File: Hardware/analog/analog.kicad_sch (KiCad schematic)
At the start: 1 part, among them Y101 25MHz

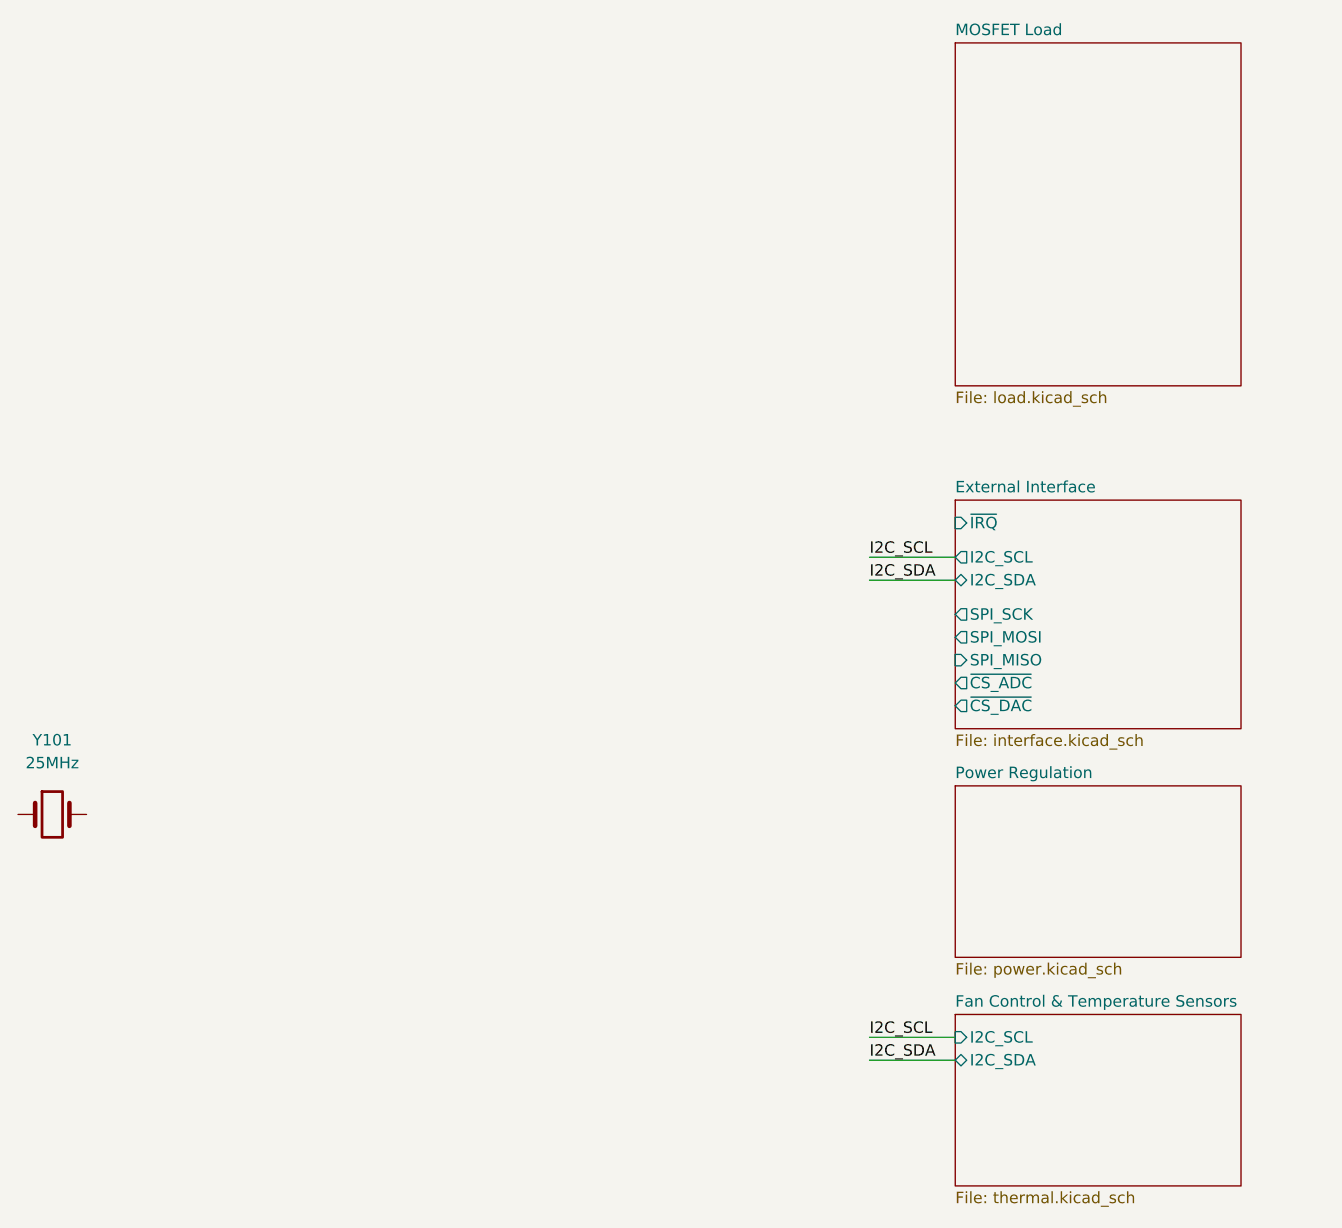
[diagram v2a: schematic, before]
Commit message: Added ADC/DAC section
- Imported the schematic for the analog DAC/ADC section, as well as the
  Vref generator and clock generator for the ADC
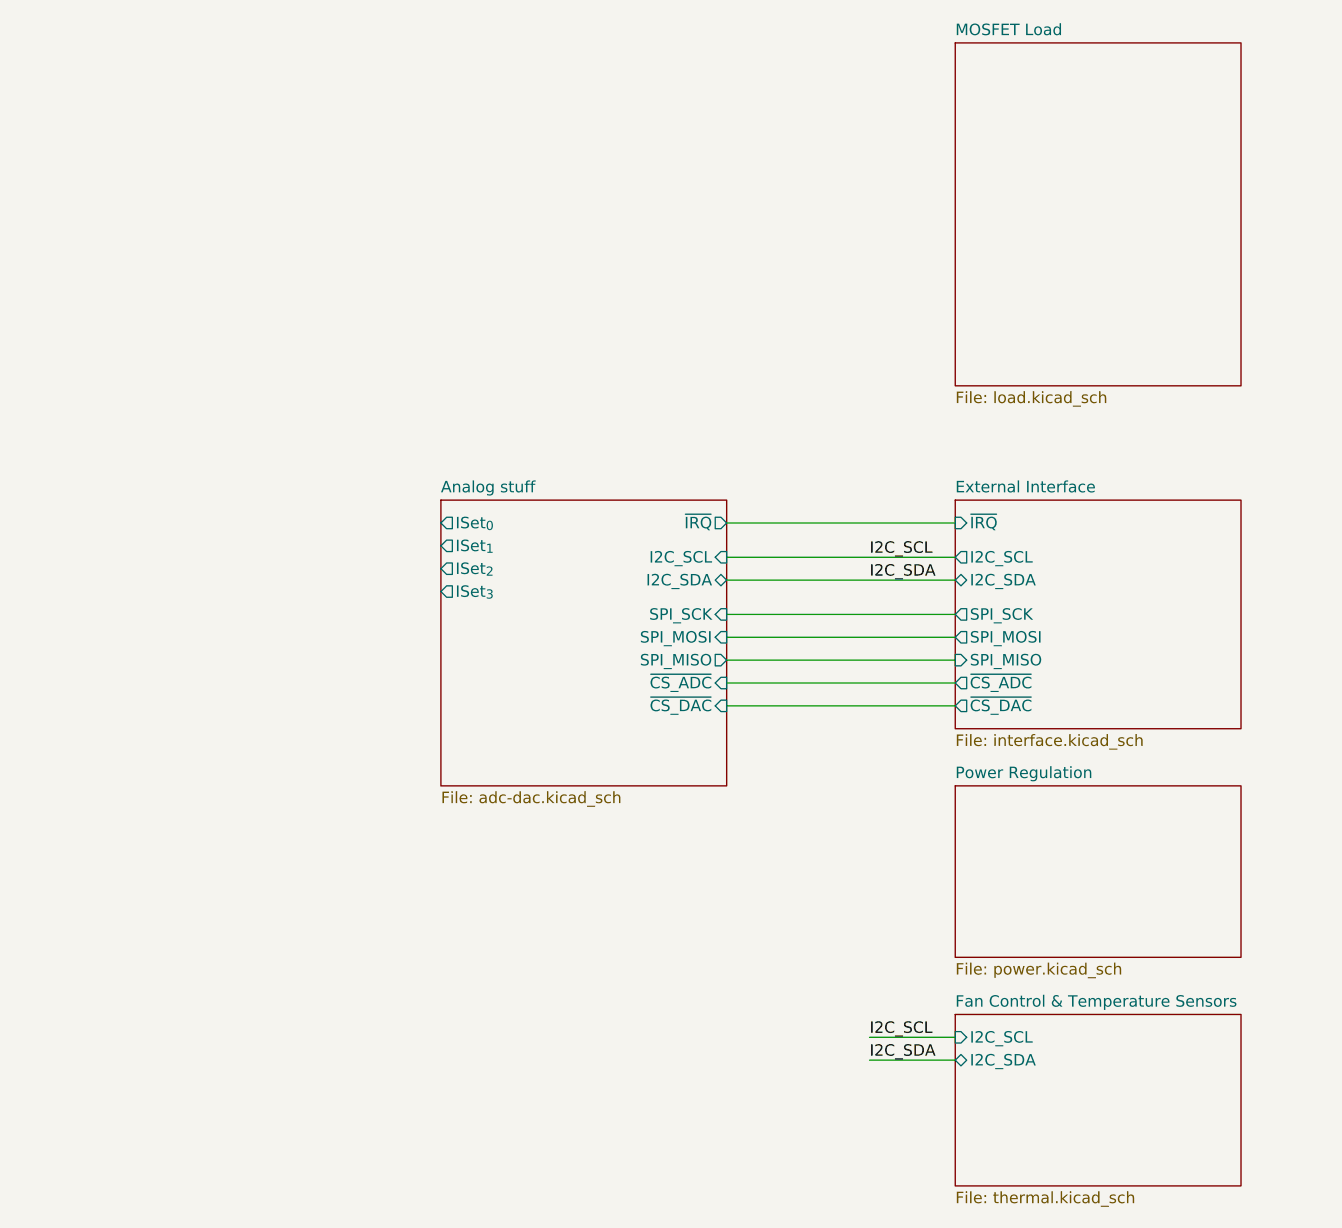
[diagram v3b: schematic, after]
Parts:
- removed Y101: 25MHz, Crystal:Crystal_SMD_SeikoEpson_TSX3225-4Pin_3.2x2.5mm_HandSoldering, symbol Device:Crystal
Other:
- added sheet Analog stuff (adc-dac.kicad_sch)

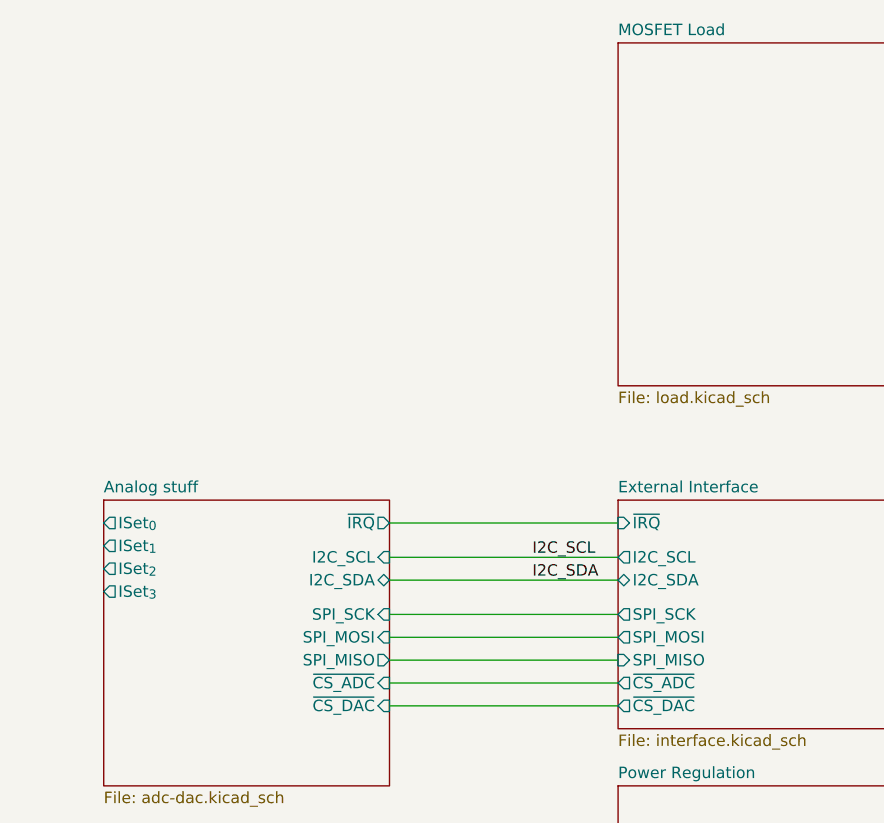
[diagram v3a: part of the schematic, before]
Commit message: Add ADC aliasing filters
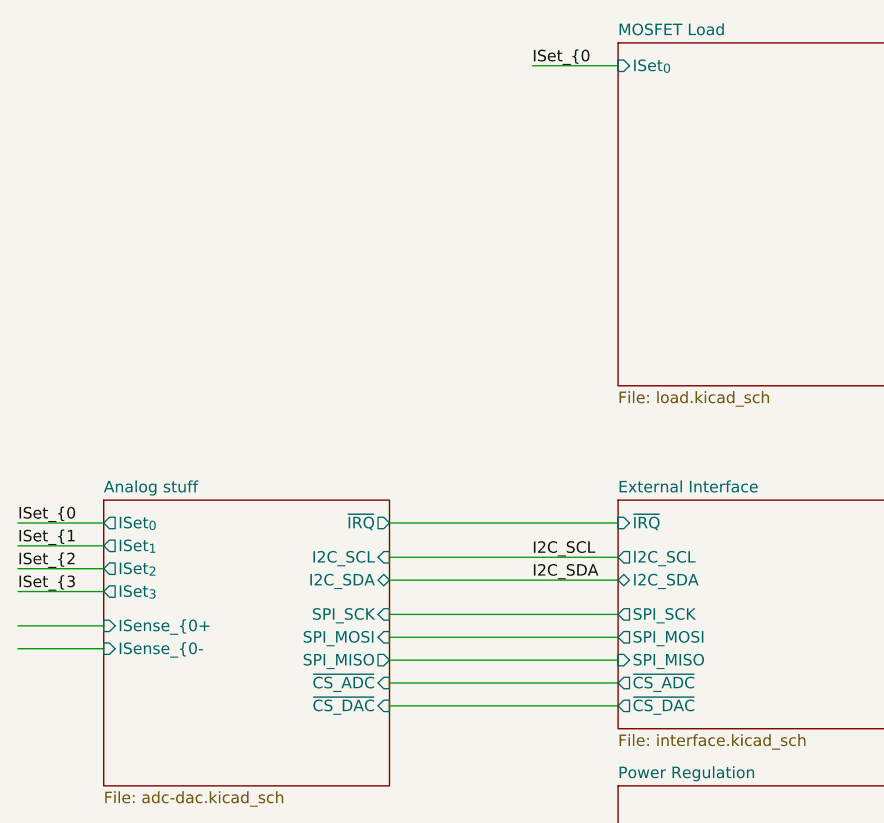
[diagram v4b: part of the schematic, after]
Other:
- sheet Analog stuff ports: added ISense_{0+, ISense_{0-; removed none
- sheet MOSFET Load ports: added ISet_{0}; removed none
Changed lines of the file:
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@@
+    (stroke (width 0) (type default) (color 0 0 0 0))
+  )
+  (wire (pts (xy 161.925 86.36) (xy 171.45 86.36))
     (stroke (width 0) (type default) (color 0 0 0 0))
   )
@@
     (stroke (width 0) (type default) (color 0 0 0 0))
   )
+  (wire (pts (xy 161.925 78.74) (xy 171.45 78.74))
+    (stroke (width 0) (type default) (color 0 0 0 0))
+  )
+  (wire (pts (xy 219.075 27.94) (xy 228.6 27.94))
+    (stroke (width 0) (type default) (color 0 0 0 0))
+  )
   (wire (pts (xy 203.2 99.06) (xy 228.6 99.06))
     (stroke (width 0) (type default) (color 0 0 0 0))
@@
     (stroke (width 0) (type default) (color 0 0 0 0))
   )
+  (wire (pts (xy 161.925 90.17) (xy 171.45 90.17))
+    (stroke (width 0) (type default) (color 0 0 0 0))
+  )
+  (wire (pts (xy 161.925 81.28) (xy 171.45 81.28))
+    (stroke (width 0) (type default) (color 0 0 0 0))
+  )
   (wire (pts (xy 203.2 96.52) (xy 228.6 96.52))
     (stroke (width 0) (type default) (color 0 0 0 0))
   )
   (wire (pts (xy 203.2 78.74) (xy 228.6 78.74))
+    (stroke (width 0) (type default) (color 0 0 0 0))
+  )
+  (wire (pts (xy 161.925 83.82) (xy 171.45 83.82))
+    (stroke (width 0) (type default) (color 0 0 0 0))
+  )
+  (wire (pts (xy 161.925 92.71) (xy 171.45 92.71))
     (stroke (width 0) (type default) (color 0 0 0 0))
   )
@@
     (effects (font (size 1.27 1.27)) (justify left bottom))
   )
+  (label "ISet_{0" (at 161.925 78.74 0)
+    (effects (font (size 1.27 1.27)) (justify left bottom))
+  )
+  (label "ISet_{2" (at 161.925 83.82 0)
+    (effects (font (size 1.27 1.27)) (justify left bottom))
+  )
   (label "I2C_SDA" (at 219.075 138.43 0)
     (effects (font (size 1.27 1.27)) (justify left bottom))
   )
+  (label "ISet_{1" (at 161.925 81.28 0)
+    (effects (font (size 1.27 1.27)) (justify left bottom))
+  )
   (label "I2C_SCL" (at 219.075 135.89 0)
+    (effects (font (size 1.27 1.27)) (justify left bottom))
+  )
+  (label "ISet_{3" (at 161.925 86.36 0)
+    (effects (font (size 1.27 1.27)) (justify left bottom))
+  )
+  (label "ISet_{0" (at 219.075 27.94 0)
     (effects (font (size 1.27 1.27)) (justify left bottom))
   )
@@
       (effects (font (size 1.27 1.27)) (justify left))
     )
+    (pin "ISense_{0+" input (at 171.45 90.17 180)
+      (effects (font (size 1.27 1.27)) (justify left))
+    )
+    (pin "ISense_{0-" input (at 171.45 92.71 180)
+      (effects (font (size 1.27 1.27)) (justify left))
+    )
   )
   (sheet (at 228.6 76.2) (size 31.75 25.4) (fields_autoplaced)
@@
     (property "Sheet file" "load.kicad_sch" (id 1) (at 228.6 64.0846 0)
       (effects (font (size 1.27 1.27)) (justify left top))
+    )
+    (pin "ISet_{0}" input (at 228.6 27.94 180)
+      (effects (font (size 1.27 1.27)) (justify left))
     )
   )
@@
       (reference "#PWR0111") (unit 1) (value "GNDA") (footprint "")
     )
+    (path "/afc218b4-6ce8-4742-9485-86399056c336/9e14dd43-0fb7-4e60-92a4-f58637916ead/c0d157c8-1a8b-4612-821d-710aff7d9c6d"
+      (reference "#PWR0112") (unit 1) (value "GND") (footprint "")
+    )
     (path "/afc218b4-6ce8-4742-9485-86399056c336/9e14dd43-0fb7-4e60-92a4-f58637916ead/e7443b7c-a1d7-4f36-833b-16f24cacd8f7"
       (reference "#PWR0113") (unit 1) (value "GND") (footprint "")
@@
       (reference "#PWR0116") (unit 1) (value "+3V3") (footprint "")
     )
+    (path "/afc218b4-6ce8-4742-9485-86399056c336/9e14dd43-0fb7-4e60-92a4-f58637916ead/6c88dc86-3465-4d2e-9993-73883be4ba7e"
+      (reference "#PWR0117") (unit 1) (value "GND") (footprint "")
+    )
+    (path "/e1649c35-e6e3-47dd-8aeb-a217676fe0ce/b5ee31ed-922a-4c24-9141-295f8bfa1a93"
+      (reference "#PWR0118") (unit 1) (value "-5VA") (footprint "")
+    )
     (path "/e1649c35-e6e3-47dd-8aeb-a217676fe0ce/d6b232d9-faf0-4a9d-8350-e9a8056ff3c8"
       (reference "#PWR0201") (unit 1) (value "GNDPWR") (footprint "")
@@
       (reference "#PWR0205") (unit 1) (value "GND") (footprint "")
     )
-    (path "/e1649c35-e6e3-47dd-8aeb-a217676fe0ce/a60ae066-97ff-47a0-9fba-29cc0372063e"
-      (reference "#PWR0206") (unit 1) (value "-5V") (footprint "")
-    )
     (path "/e1649c35-e6e3-47dd-8aeb-a217676fe0ce/2d7d7fb0-6be6-4904-b2db-292874b5df9d"
       (reference "#PWR0207") (unit 1) (value "GND") (footprint "")
@@
       (reference "#PWR0610") (unit 1) (value "+3V3A") (footprint "")
     )
+    (path "/afc218b4-6ce8-4742-9485-86399056c336/b66a66f9-d9ef-45b0-9567-e730c3557aa4"
+      (reference "#PWR0611") (unit 1) (value "GND") (footprint "")
+    )
+    (path "/afc218b4-6ce8-4742-9485-86399056c336/2573d9c5-2471-4f25-8270-a0e593074a8c"
+      (reference "#PWR0612") (unit 1) (value "GND") (footprint "")
+    )
+    (path "/afc218b4-6ce8-4742-9485-86399056c336/f403f9e6-efc9-4047-9236-8b8d1b948936"
+      (reference "#PWR0613") (unit 1) (value "GND") (footprint "")
+    )
+    (path "/afc218b4-6ce8-4742-9485-86399056c336/465cf86d-1af3-4db2-a415-e171566b35f4"
+      (reference "#PWR0614") (unit 1) (value "GND") (footprint "")
+    )
     (path "/e1649c35-e6e3-47dd-8aeb-a217676fe0ce/82c2c0cf-1141-4c1a-8013-130daf3cd355"
       (reference "C201") (unit 1) (value "1nF") (footprint "Capacitor_SMD:C_0805_2012Metric_Pad1.18x1.45mm_HandSolder")
@@
       (reference "C607") (unit 1) (value "100nF") (footprint "Capacitor_SMD:C_0805_2012Metric_Pad1.18x1.45mm_HandSolder")
     )
+    (path "/afc218b4-6ce8-4742-9485-86399056c336/a9cbcc4c-e154-40bd-aeaf-9f0fde05fcfa"
+      (reference "C608") (unit 1) (value "100nF") (footprint "Capacitor_SMD:C_0805_2012Metric_Pad1.18x1.45mm_HandSolder")
+    )
+    (path "/afc218b4-6ce8-4742-9485-86399056c336/48997eaf-129a-45f6-bb7f-bd304f510a8a"
+      (reference "C609") (unit 1) (value "100nF") (footprint "Capacitor_SMD:C_0805_2012Metric_Pad1.18x1.45mm_HandSolder")
+    )
+    (path "/afc218b4-6ce8-4742-9485-86399056c336/f2c35989-6d1a-468d-9f92-920b43f181d6"
+      (reference "C610") (unit 1) (value "100nF") (footprint "Capacitor_SMD:C_0805_2012Metric_Pad1.18x1.45mm_HandSolder")
+    )
+    (path "/afc218b4-6ce8-4742-9485-86399056c336/eeaf01d6-cc55-4e1b-b739-01bd26118771"
+      (reference "C611") (unit 1) (value "100nF") (footprint "Capacitor_SMD:C_0805_2012Metric_Pad1.18x1.45mm_HandSolder")
+    )
+    (path "/afc218b4-6ce8-4742-9485-86399056c336/4d7e1fb4-46db-41ed-8e94-83c891b92879"
+      (reference "C612") (unit 1) (value "100nF") (footprint "Capacitor_SMD:C_0805_2012Metric_Pad1.18x1.45mm_HandSolder")
+    )
+    (path "/afc218b4-6ce8-4742-9485-86399056c336/0a1ffbe8-ffd7-4ffc-bcbb-15f65db6ae79"
+      (reference "C613") (unit 1) (value "100nF") (footprint "Capacitor_SMD:C_0805_2012Metric_Pad1.18x1.45mm_HandSolder")
+    )
+    (path "/afc218b4-6ce8-4742-9485-86399056c336/b4b9efa9-a4b8-4778-8d76-b8a8ee4c0301"
+      (reference "C614") (unit 1) (value "100nF") (footprint "Capacitor_SMD:C_0805_2012Metric_Pad1.18x1.45mm_HandSolder")
+    )
+    (path "/afc218b4-6ce8-4742-9485-86399056c336/1155209e-63c6-428b-b454-9b40b5f6cadc"
+      (reference "C615") (unit 1) (value "100nF") (footprint "Capacitor_SMD:C_0805_2012Metric_Pad1.18x1.45mm_HandSolder")
+    )
     (path "/afc218b4-6ce8-4742-9485-86399056c336/9e14dd43-0fb7-4e60-92a4-f58637916ead/30cb2ddc-3798-4714-8b15-0ad4a13517e7"
       (reference "C701") (unit 1) (value "100nF") (footprint "Capacitor_SMD:C_0805_2012Metric_Pad1.18x1.45mm_HandSolder")
@@
       (reference "R601") (unit 1) (value "10k") (footprint "Resistor_SMD:R_0805_2012Metric_Pad1.20x1.40mm_HandSolder")
     )
+    (path "/afc218b4-6ce8-4742-9485-86399056c336/050baef7-7cf4-49c8-b7c3-de1bdb63eec3"
+      (reference "R602") (unit 1) (value "1k") (footprint "Resistor_SMD:R_0805_2012Metric_Pad1.20x1.40mm_HandSolder")
+    )
+    (path "/afc218b4-6ce8-4742-9485-86399056c336/31af6869-0913-403b-86b5-6085a4a63a36"
+      (reference "R603") (unit 1) (value "1k") (footprint "Resistor_SMD:R_0805_2012Metric_Pad1.20x1.40mm_HandSolder")
+    )
+    (path "/afc218b4-6ce8-4742-9485-86399056c336/d48365cd-a437-42d5-84c6-0293b43a0751"
+      (reference "R604") (unit 1) (value "1k") (footprint "Resistor_SMD:R_0805_2012Metric_Pad1.20x1.40mm_HandSolder")
+    )
+    (path "/afc218b4-6ce8-4742-9485-86399056c336/31d22cc0-7690-4229-bb31-d15edfab25a5"
+      (reference "R605") (unit 1) (value "1k") (footprint "Resistor_SMD:R_0805_2012Metric_Pad1.20x1.40mm_HandSolder")
+    )
+    (path "/afc218b4-6ce8-4742-9485-86399056c336/cd40ff8e-1a6d-4aab-b5e0-605a56259c6c"
+      (reference "R606") (unit 1) (value "1k") (footprint "Resistor_SMD:R_0805_2012Metric_Pad1.20x1.40mm_HandSolder")
+    )
+    (path "/afc218b4-6ce8-4742-9485-86399056c336/2e025533-eef7-40be-ae61-ecf3105ea461"
+      (reference "R607") (unit 1) (value "1k") (footprint "Resistor_SMD:R_0805_2012Metric_Pad1.20x1.40mm_HandSolder")
+    )
+    (path "/afc218b4-6ce8-4742-9485-86399056c336/8cb1209a-d8db-4020-b122-b6b1dd134378"
+      (reference "R608") (unit 1) (value "1k") (footprint "Resistor_SMD:R_0805_2012Metric_Pad1.20x1.40mm_HandSolder")
+    )
+    (path "/afc218b4-6ce8-4742-9485-86399056c336/8c6805f8-0670-4b62-9836-64a78c24f573"
+      (reference "R609") (unit 1) (value "1k") (footprint "Resistor_SMD:R_0805_2012Metric_Pad1.20x1.40mm_HandSolder")
+    )
     (path "/afc218b4-6ce8-4742-9485-86399056c336/9e14dd43-0fb7-4e60-92a4-f58637916ead/50fb8134-09ae-4bde-8de4-6edf60d4d347"
